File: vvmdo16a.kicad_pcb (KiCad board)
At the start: 2 copper layers, 35 x 60 mm, 18 parts, among them J1 517-N2508-6002RB, J2 517-N2520-6002RB, J3 Conn_02x01, J4 Conn_02x01, SW1 220ADC16, U1 PCA9685PW, U2 ULN2803A, U3 ULN2803A

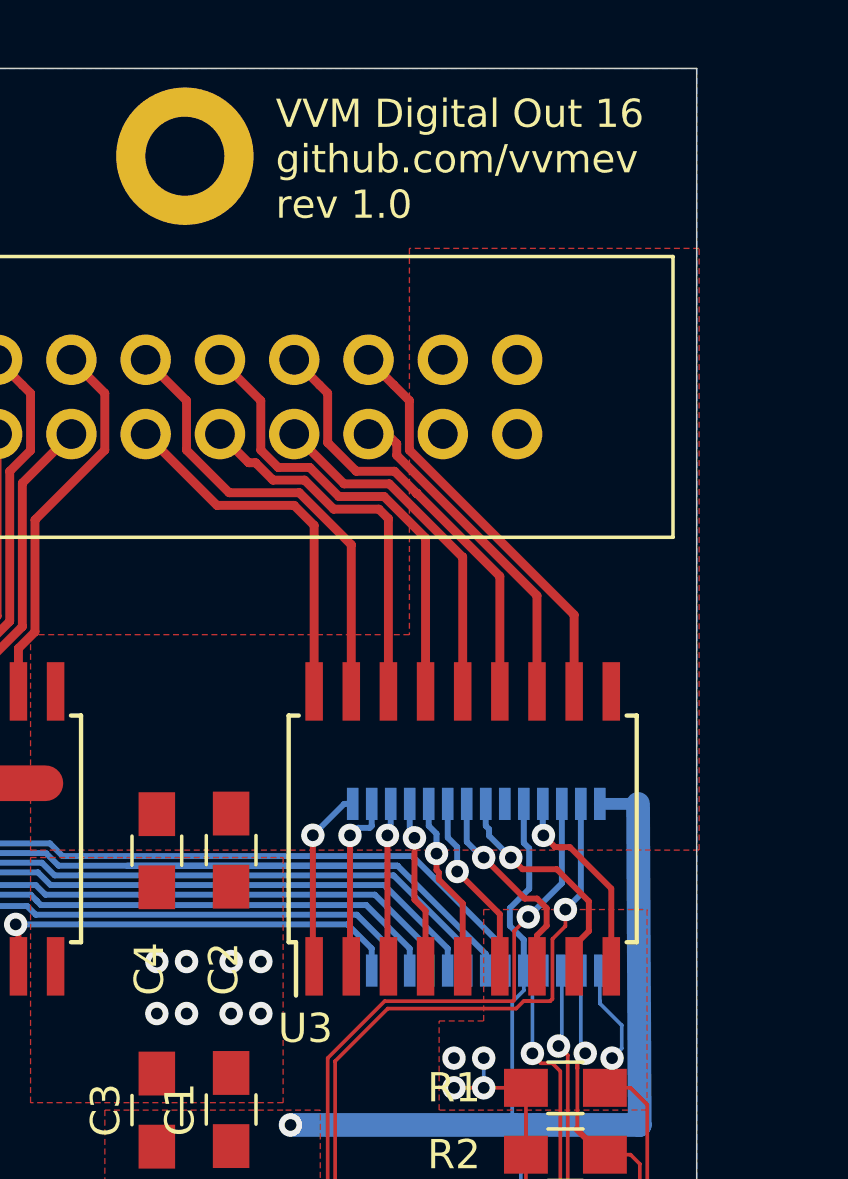
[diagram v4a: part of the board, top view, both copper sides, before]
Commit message: Tie A4 to GND instead of +3V3
This selects addresses 0x60-0x6f for the IO controller.

Fixes #1
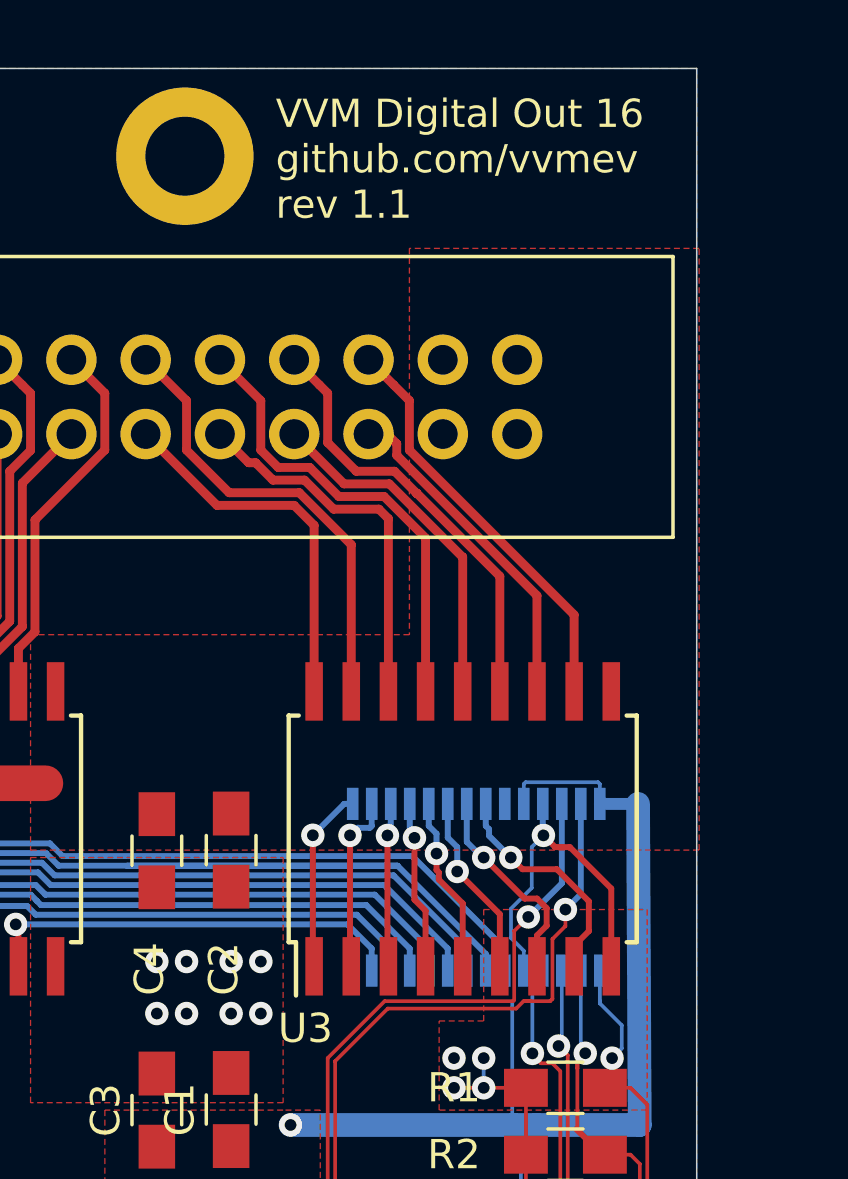
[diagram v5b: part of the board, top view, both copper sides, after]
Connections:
- U1 pad 5: +3V3 -> GND
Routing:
- net GND: track 17.2 -> 22.4 mm
- net +3V3: track 71.8 -> 68.3 mm
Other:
- board text added: "VVM Digital Out 16 github.com/vvmev rev 1.1"
- board text removed: "VVM Digital Out 16 github.com/vvmev rev 1.0"
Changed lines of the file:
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@@
     (thickness 1.6)
     (drawings 9)
-    (tracks 382)
+    (tracks 384)
     (zones 0)
     (modules 18)
@@
       (net 41 /A3))
     (pad 5 smd rect (at -2.85 1.625 90) (size 1.1 0.4) (layers B.Cu B.Paste B.Mask)
-      (net 1 +3V3))
+      (net 2 GND))
     (pad 6 smd rect (at -2.85 0.975 90) (size 1.1 0.4) (layers B.Cu B.Paste B.Mask)
       (net 22 /PWM1))
@@
     (effects (font (size 1.5 1.5) (thickness 0.3)))
   )
-  (gr_text "VVM Digital Out 16\ngithub.com/vvmev\nrev 1.0" (at 149.606 70.104) (layer F.SilkS)
+  (gr_text "VVM Digital Out 16\ngithub.com/vvmev\nrev 1.1" (at 149.606 70.104) (layer F.SilkS)
     (effects (font (size 0.9652 0.9652) (thickness 0.1524)) (justify left))
   )
@@
   (segment (start 142.24 113.792) (end 144.526 111.506) (width 1.2192) (layer F.Cu) (net 1))
   (segment (start 144.526 111.506) (end 144.526 105.664) (width 1.2192) (layer F.Cu) (net 1))
-  (segment (start 157.613399 96.313729) (end 158.089 96.78933) (width 0.2032) (layer B.Cu) (net 1))
-  (segment (start 157.613399 95.710271) (end 157.613399 96.313729) (width 0.2032) (layer B.Cu) (net 1))
-  (segment (start 158.089 96.78933) (end 158.089 97.846) (width 0.2032) (layer B.Cu) (net 1))
-  (segment (start 158.273604 93.666536) (end 158.273604 95.050066) (width 0.2032) (layer B.Cu) (net 1))
-  (segment (start 158.089 93.481932) (end 158.273604 93.666536) (width 0.2032) (layer B.Cu) (net 1))
-  (segment (start 158.273604 95.050066) (end 157.613399 95.710271) (width 0.2032) (layer B.Cu) (net 1))
-  (segment (start 158.089 92.146) (end 158.089 93.481932) (width 0.2032) (layer B.Cu) (net 1))
   (segment (start 160.689 92.146) (end 161.996 92.146) (width 0.4064) (layer B.Cu) (net 1))
   (via (at 150.114 103.124) (size 0.8) (drill 0.4) (layers F.Cu B.Cu) (net 1))
   (segment (start 157.693609 98.918391) (end 157.693609 103.083609) (width 0.127) (layer B.Cu) (net 1))
-  (segment (start 158.089 98.523) (end 157.693609 98.918391) (width 0.127) (layer B.Cu) (net 1))
   (segment (start 157.693609 103.083609) (end 157.734 103.124) (width 0.127) (layer B.Cu) (net 1))
-  (segment (start 158.089 97.846) (end 158.089 98.523) (width 0.127) (layer B.Cu) (net 1))
   (segment (start 157.734 103.124) (end 150.114 103.124) (width 0.8128) (layer B.Cu) (net 1))
   (segment (start 157.988 124.46) (end 157.988 116.84) (width 0.127) (layer B.Cu) (net 1))
@@
   (segment (start 158.520436 103.124) (end 157.734 103.124) (width 0.8128) (layer B.Cu) (net 1))
   (segment (start 161.996 92.146) (end 162.052 103.124) (width 0.8128) (layer B.Cu) (net 1))
+  (segment (start 158.089 91.469) (end 158.089 92.146) (width 0.127) (layer B.Cu) (net 1))
+  (segment (start 158.152501 91.405499) (end 158.089 91.469) (width 0.127) (layer B.Cu) (net 1))
+  (segment (start 160.625499 91.405499) (end 158.152501 91.405499) (width 0.127) (layer B.Cu) (net 1))
+  (segment (start 160.689 91.469) (end 160.625499 91.405499) (width 0.127) (layer B.Cu) (net 1))
+  (segment (start 160.689 92.146) (end 160.689 91.469) (width 0.127) (layer B.Cu) (net 1))
   (via (at 155.702 100.838) (size 0.8) (drill 0.4) (layers F.Cu B.Cu) (net 2))
   (segment (start 158.739 93.201602) (end 158.7604 93.223002) (width 0.2032) (layer B.Cu) (net 2))
@@
   (via (at 149.098 97.536) (size 0.8) (drill 0.4) (layers F.Cu B.Cu) (net 2))
   (via (at 149.098 99.314) (size 0.8) (drill 0.4) (layers F.Cu B.Cu) (net 2))
+  (segment (start 157.651499 96.731499) (end 158.089 97.169) (width 0.127) (layer B.Cu) (net 2))
+  (segment (start 157.651499 95.728559) (end 157.651499 96.731499) (width 0.127) (layer B.Cu) (net 2))
+  (segment (start 158.360401 95.019657) (end 157.651499 95.728559) (width 0.127) (layer B.Cu) (net 2))
+  (segment (start 158.089 97.169) (end 158.089 97.846) (width 0.127) (layer B.Cu) (net 2))
+  (segment (start 158.360401 93.623001) (end 158.360401 95.019657) (width 0.127) (layer B.Cu) (net 2))
+  (segment (start 158.7604 93.223002) (end 158.360401 93.623001) (width 0.127) (layer B.Cu) (net 2))
   (via (at 158.242 96.012) (size 0.8) (drill 0.4) (layers F.Cu B.Cu) (net 3))
   (segment (start 159.389 94.865) (end 158.242 96.012) (width 0.2032) (layer B.Cu) (net 3))
